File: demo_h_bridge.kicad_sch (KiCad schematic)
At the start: 2 parts, among them Q1 NMOS, Q2 NMOS

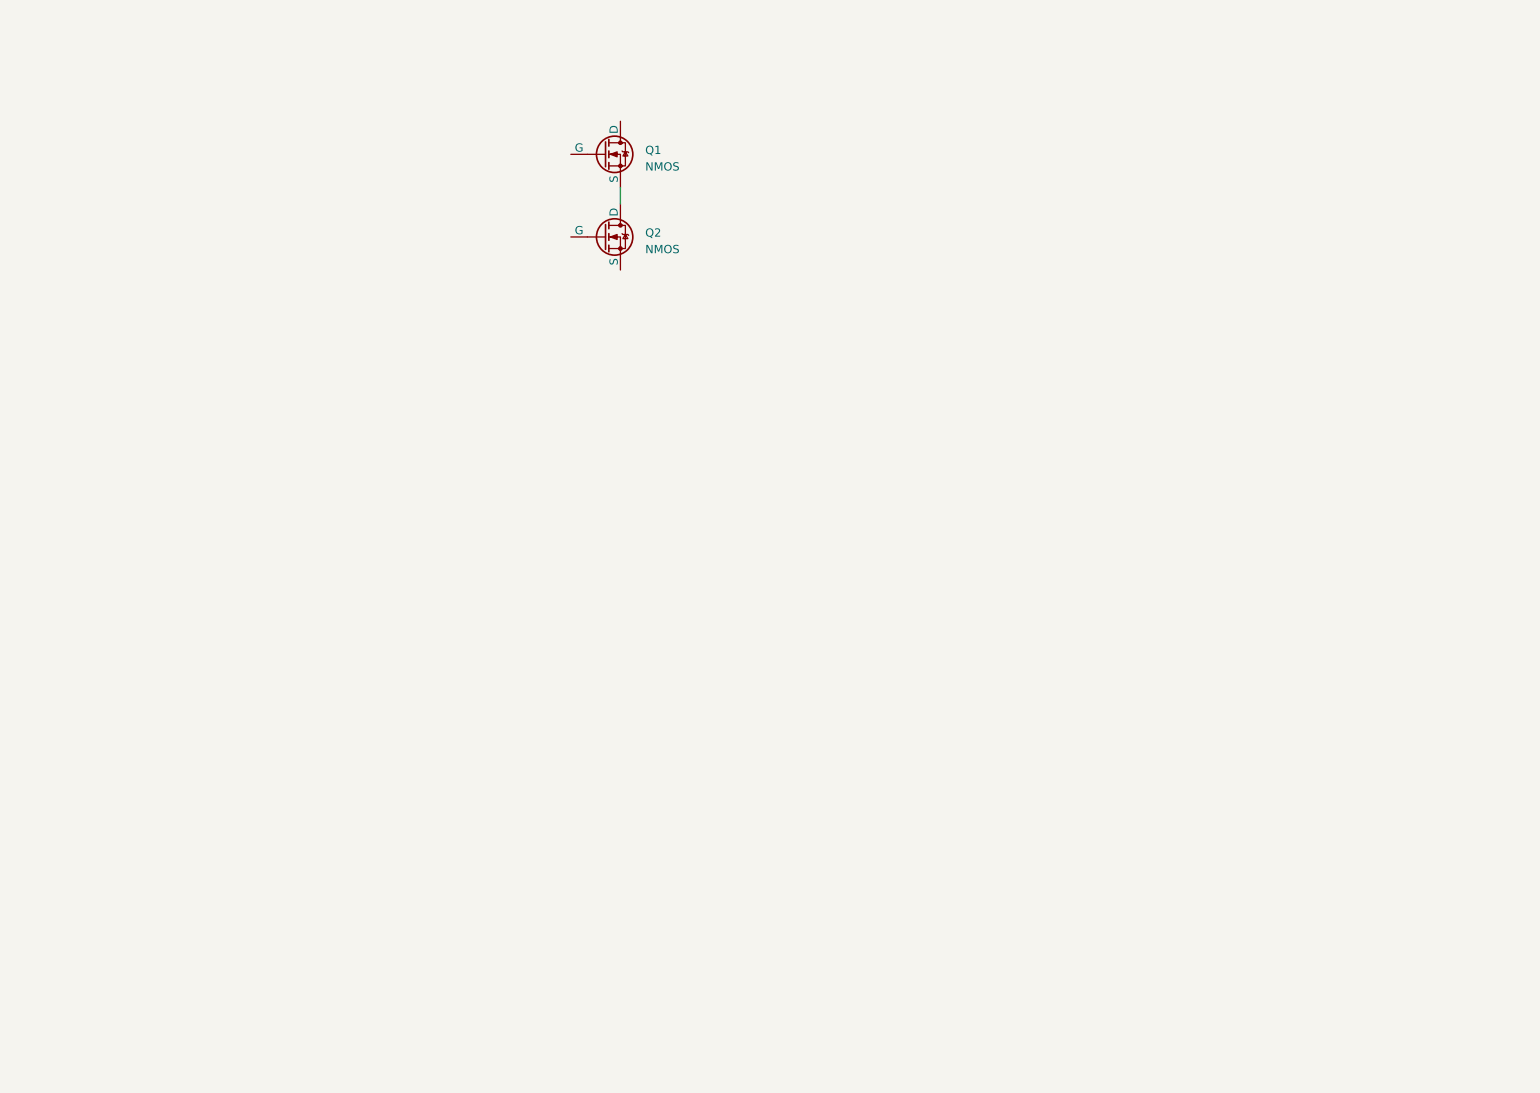
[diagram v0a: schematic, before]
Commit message: buck/boost converter topology
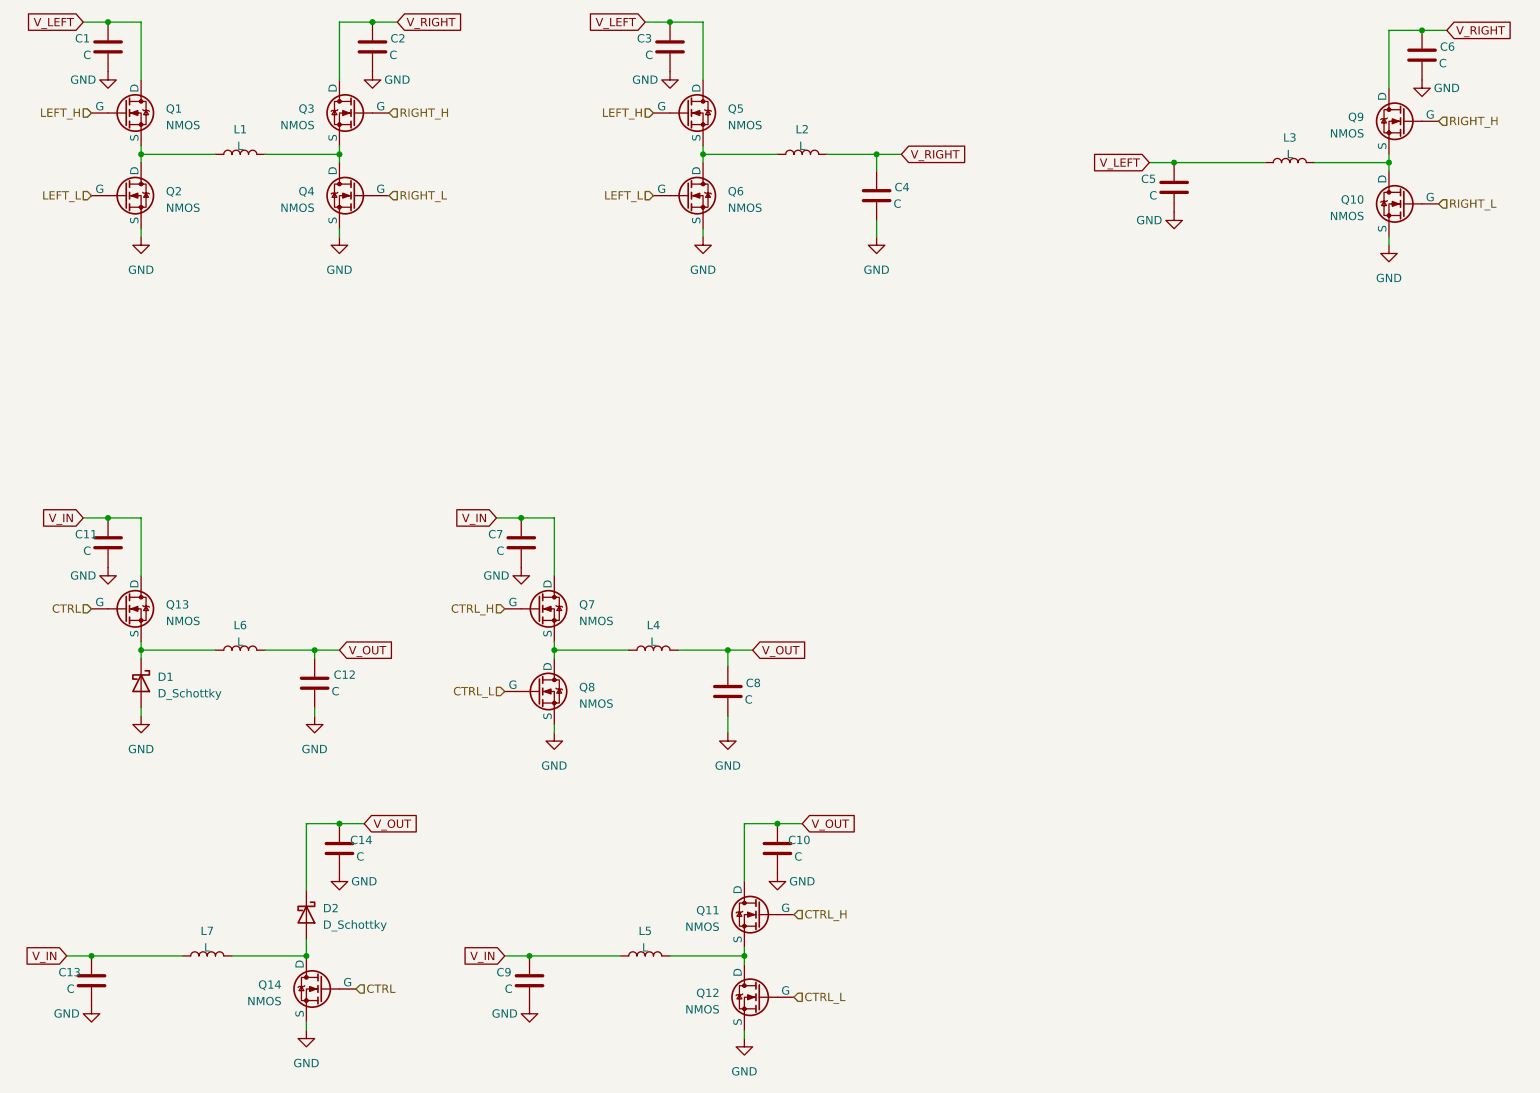
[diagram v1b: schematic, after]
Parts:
- added C1, C10, C11, C12, C13, C14, C2, C3, C4, C5, C6, C7, C8, C9: C, symbol Device:C
- added D1, D2: D_Schottky, symbol Device:D_Schottky
- added L1, L2, L3, L4, L5, L6, L7: L, symbol Device:L
- added Q10, Q11, Q12, Q13, Q14, Q3, Q4, Q5, Q6, Q7, Q8, Q9: NMOS, symbol Simulation_SPICE:NMOS
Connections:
- net at Q1.3 (S), Q2.1 (D): now also L1.1
- net LEFT_L: now reaches Q2.2 (G)
- net LEFT_L: now also Q6.2 (G)
- net GND: now reaches Q2.3 (S)
- net GND: now also C1.2, C10.2, C11.2, C12.2, C13.2, C14.2, C2.2, C3.2, C4.2, C5.2, C6.2, C7.2, C8.2, C9.2, D1.2 (A), Q10.3 (S), Q12.3 (S), Q14.3 (S), Q4.3 (S), Q6.3 (S), Q8.3 (S)
- net V_LEFT: now reaches Q1.1 (D)
- net V_LEFT: now also C1.1, C3.1, C5.1, L3.1, Q5.1 (D)
- net LEFT_H: now reaches Q1.2 (G)
- net LEFT_H: now also Q5.2 (G)
- new net: D1.1 (K), L6.1, Q13.3 (S)
- new net: L2.1, Q5.3 (S), Q6.1 (D)
- new net: D2.2 (A), L7.2, Q14.1 (D)
- new net: L1.2, Q3.3 (S), Q4.1 (D)
- new net: L3.2, Q10.1 (D), Q9.3 (S)
- new net: L5.2, Q11.3 (S), Q12.1 (D)
- new net: L4.1, Q7.3 (S), Q8.1 (D)
- new net CTRL: Q13.2 (G), Q14.2 (G)
- new net CTRL_H: Q11.2 (G), Q7.2 (G)
- new net CTRL_L: Q12.2 (G), Q8.2 (G)
- new net RIGHT_H: Q3.2 (G), Q9.2 (G)
- new net RIGHT_L: Q10.2 (G), Q4.2 (G)
- new net V_IN: C11.1, C13.1, C7.1, C9.1, L5.1, L7.1, Q13.1 (D), Q7.1 (D)
- new net V_OUT: C10.1, C12.1, C14.1, C8.1, D2.1 (K), L4.2, L6.2, Q11.1 (D)
- new net V_RIGHT: C2.1, C4.1, C6.1, L2.2, Q3.1 (D), Q9.1 (D)
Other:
- moved on the sheet: Q1, Q2
